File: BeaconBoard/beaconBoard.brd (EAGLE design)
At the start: 101.6 x 76.2 mm, 33 parts, among them IC1 7805TV, Q1 2N3904

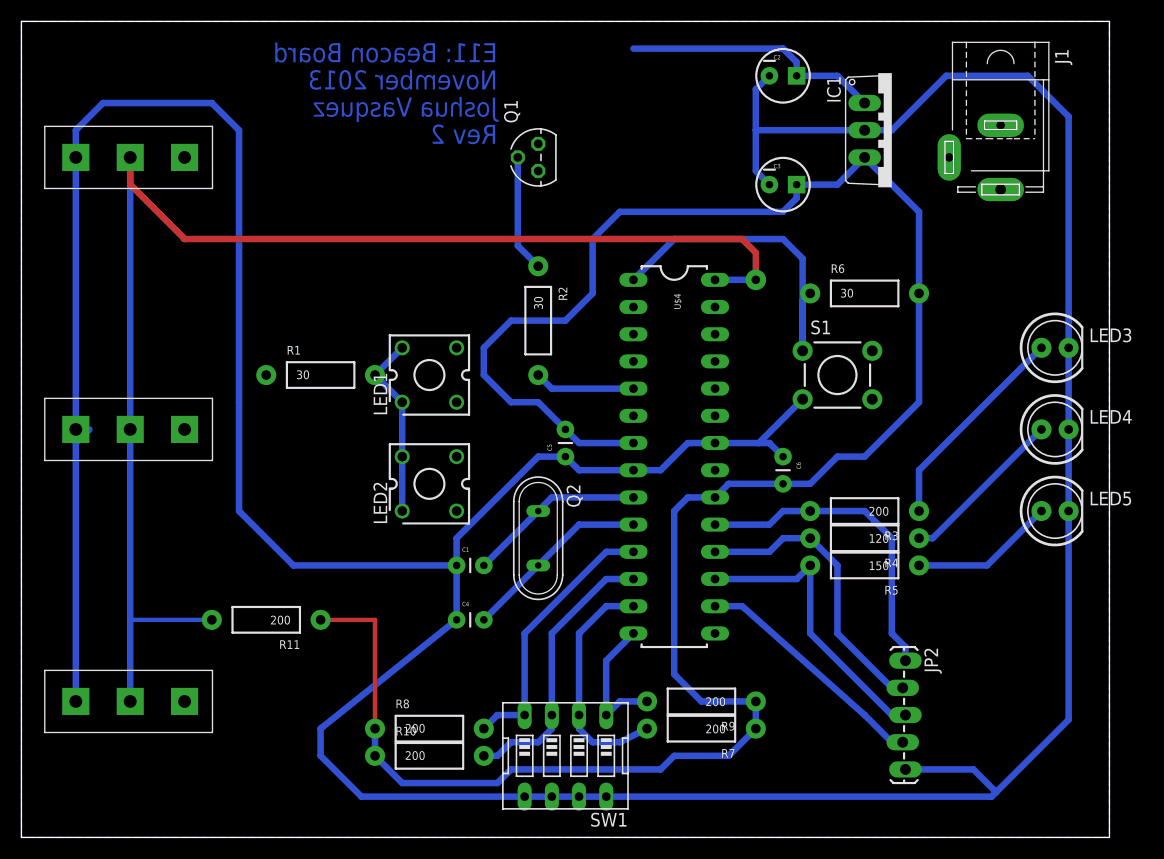
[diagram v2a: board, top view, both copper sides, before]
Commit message: Reroute for new transistor configuration
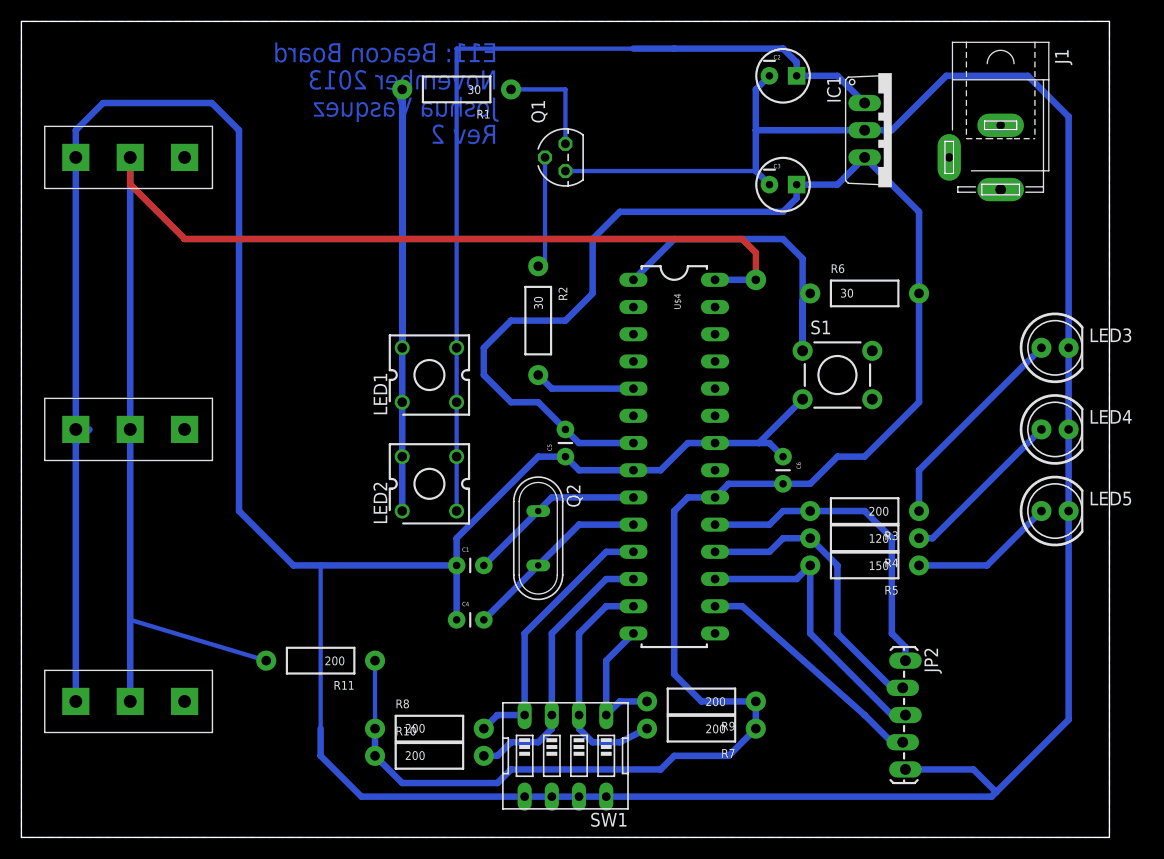
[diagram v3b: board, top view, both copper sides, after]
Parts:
- moved R1 29.5 mm to (40.6, 69.8), turned to 180 degrees
- moved R11 6.35 mm to (27.9, 16.5)
- moved Q1 2.54 mm to (50.8, 63.5)
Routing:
- net VDD: track 24.4 -> 87.9 mm
- net N$3: track 17.3 -> 63.5 mm
- net GND: track 381.3 -> 398.1 mm
- net N$1: track 0.00 -> 10.2 mm
- net VCC: track 200.8 -> 194.4 mm
- net BUMPER: track 128.4 -> 134.0 mm
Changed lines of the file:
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@@
 <element name="U$3" library="hmcfabstudio" package="D2F-L" value="DF2-L" x="5.08" y="38.1"/>
 <element name="U$4" library="hmcfabstudio" package="DIL28-3" value="ATMEGA328" x="60.96" y="35.56" rot="R270"/>
-<element name="Q1" library="transistor-small-signal" package="TO92D" value="2N3904" x="48.26" y="63.5" rot="R90"/>
+<element name="Q1" library="transistor-small-signal" package="TO92D" value="2N3904" x="50.8" y="63.5" rot="R90"/>
 <element name="J1" library="con-jack" package="SPC4078" value="" x="91.44" y="63.5" rot="R270">
 <attribute name="OC_NEWARK" value="unknown" x="91.44" y="63.5" size="1.778" layer="27" rot="R270" display="off"/>
@@
 <element name="LED1" library="led" package="CP41B" value="" x="38.1" y="43.18" rot="R90"/>
 <element name="LED2" library="led" package="CP41B" value="" x="38.1" y="33.02" rot="R90"/>
-<element name="R1" library="SparkFun-Resistors" package="AXIAL-0.4" value="30" x="27.94" y="43.18"/>
+<element name="R1" library="SparkFun-Resistors" package="AXIAL-0.4" value="30" x="40.64" y="69.85" rot="R180"/>
 <element name="R2" library="SparkFun-Resistors" package="AXIAL-0.4" value="30" x="48.26" y="48.26" rot="R270"/>
 <element name="R3" library="SparkFun-Resistors" package="AXIAL-0.4" value="200" x="78.74" y="30.48" rot="R180"/>
@@
 <element name="C6" library="SparkFun-Passives" package="CAP-PTH-SMALL" value="" x="71.12" y="35.56" rot="R270"/>
 <element name="JP2" library="SparkFun-Connectors" package="1X05_LOCK_LONGPADS" value="" x="82.55" y="16.51" rot="R270"/>
-<element name="R11" library="SparkFun-Resistors" package="AXIAL-0.4" value="200" x="22.86" y="20.32" rot="R180"/>
+<element name="R11" library="SparkFun-Resistors" package="AXIAL-0.4" value="200" x="27.94" y="16.51" rot="R180"/>
 </elements>
 <signals>
@@
 <wire x1="45.72" y1="6.35" x2="44.45" y2="5.08" width="0.6096" layer="16"/>
 <contactref element="R11" pad="P$1"/>
-<wire x1="27.94" y1="20.32" x2="33.02" y2="20.32" width="0.4064" layer="1"/>
-<wire x1="33.02" y1="20.32" x2="33.02" y2="10.16" width="0.4064" layer="1"/>
+<wire x1="33.02" y1="16.51" x2="33.02" y2="7.62" width="0.4064" layer="16"/>
 </signal>
 <signal name="GND">
@@
 <wire x1="71.12" y1="35.56" x2="69.85" y2="36.83" width="0.6096" layer="16"/>
 <wire x1="69.85" y1="36.83" x2="68.8594" y2="36.83" width="0.6096" layer="16"/>
-<wire x1="20.32" y1="40.64" x2="20.32" y2="30.48" width="0.6096" layer="16"/>
 <wire x1="20.32" y1="30.48" x2="25.4" y2="25.4" width="0.6096" layer="16"/>
-<wire x1="25.4" y1="25.4" x2="40.64" y2="25.4" width="0.6096" layer="16"/>
+<wire x1="25.4" y1="25.4" x2="27.94" y2="25.4" width="0.6096" layer="16"/>
+<wire x1="27.94" y1="25.4" x2="40.64" y2="25.4" width="0.6096" layer="16"/>
 <wire x1="40.64" y1="25.4" x2="40.64" y2="20.32" width="0.6096" layer="16"/>
-<wire x1="40.64" y1="20.32" x2="27.94" y2="10.16" width="0.6096" layer="16"/>
 <wire x1="27.94" y1="10.16" x2="27.94" y2="7.62" width="0.6096" layer="16"/>
 <wire x1="27.94" y1="7.62" x2="31.75" y2="3.81" width="0.6096" layer="16"/>
@@
 <wire x1="5.08" y1="12.7" x2="5.08" y2="36.83" width="0.6096" layer="16"/>
 <wire x1="5.08" y1="36.83" x2="6.35" y2="38.1" width="0.6096" layer="16"/>
-<wire x1="20.32" y1="40.64" x2="20.32" y2="66.04" width="0.6096" layer="16"/>
+<wire x1="20.32" y1="30.48" x2="20.32" y2="66.04" width="0.6096" layer="16"/>
 <wire x1="20.32" y1="66.04" x2="17.78" y2="68.58" width="0.6096" layer="16"/>
 <wire x1="17.78" y1="68.58" x2="7.62" y2="68.58" width="0.6096" layer="16"/>
@@
 </polygon>
 <contactref element="Q1" pad="E"/>
-<wire x1="68.58" y1="62.23" x2="48.26" y2="62.23" width="0" layer="19" extent="16-16"/>
+<wire x1="50.8" y1="62.23" x2="68.58" y2="62.23" width="0.4064" layer="16"/>
+<wire x1="27.94" y1="10.16" x2="27.94" y2="25.4" width="0.4064" layer="16"/>
 <wire x1="5.08" y1="36.83" x2="5.08" y2="38.1" width="0" layer="19" extent="16-16"/>
 </signal>
@@
 <wire x1="78.74" y1="68.58" x2="76.2" y2="71.12" width="0.6096" layer="16"/>
 <wire x1="76.2" y1="71.12" x2="72.39" y2="71.12" width="0.6096" layer="16"/>
-<wire x1="57.15" y1="73.66" x2="71.12" y2="73.66" width="0.6096" layer="16"/>
+<wire x1="57.15" y1="73.66" x2="60.96" y2="73.66" width="0.6096" layer="16"/>
+<wire x1="60.96" y1="73.66" x2="71.12" y2="73.66" width="0.6096" layer="16"/>
 <wire x1="72.39" y1="71.12" x2="72.39" y2="72.39" width="0.6096" layer="16"/>
 <wire x1="72.39" y1="72.39" x2="71.12" y2="73.66" width="0.6096" layer="16"/>
@@
 <contactref element="LED2" pad="2"/>
 <contactref element="LED2" pad="3"/>
-<wire x1="40.64" y1="45.72" x2="57.15" y2="73.66" width="0" layer="19" extent="16-16"/>
-<wire x1="40.64" y1="40.64" x2="40.64" y2="45.72" width="0" layer="19" extent="1-1"/>
+<wire x1="40.64" y1="30.48" x2="40.64" y2="45.72" width="0.4064" layer="16"/>
+<wire x1="40.64" y1="45.72" x2="40.64" y2="73.66" width="0.4064" layer="16"/>
+<wire x1="40.64" y1="73.66" x2="60.96" y2="73.66" width="0.4064" layer="16"/>
 <wire x1="40.64" y1="35.56" x2="40.64" y2="40.64" width="0" layer="19" extent="1-1"/>
-<wire x1="40.64" y1="30.48" x2="40.64" y2="35.56" width="0" layer="19" extent="1-1"/>
+<wire x1="40.64" y1="45.72" x2="40.64" y2="40.64" width="0" layer="19" extent="1-1"/>
 </signal>
 <signal name="N$3">
@@
 <contactref element="LED2" pad="1"/>
 <contactref element="R1" pad="P$2"/>
-<wire x1="33.02" y1="43.18" x2="35.56" y2="45.72" width="0.6096" layer="16"/>
-<wire x1="35.56" y1="40.64" x2="33.02" y2="43.18" width="0.6096" layer="16"/>
+<wire x1="35.56" y1="69.85" x2="35.56" y2="45.72" width="0.6096" layer="16"/>
+<wire x1="35.56" y1="40.64" x2="35.56" y2="69.85" width="0.6096" layer="16"/>
 <wire x1="35.56" y1="35.56" x2="35.56" y2="40.64" width="0.6096" layer="16"/>
 <wire x1="35.56" y1="35.56" x2="35.56" y2="30.48" width="0.6096" layer="16"/>
@@
 <contactref element="Q1" pad="B"/>
 <contactref element="R2" pad="P$1"/>
-<wire x1="48.26" y1="53.34" x2="46.355" y2="55.245" width="0.6096" layer="16"/>
-<wire x1="46.355" y1="55.245" x2="46.355" y2="63.5" width="0.6096" layer="16"/>
+<wire x1="48.26" y1="53.34" x2="48.895" y2="53.34" width="0.4064" layer="16"/>
+<wire x1="48.895" y1="53.34" x2="48.895" y2="63.5" width="0.4064" layer="16"/>
 </signal>
 <signal name="N$5">
@@
 <wire x1="10.16" y1="60.96" x2="10.16" y2="63.5" width="0.6096" layer="1"/>
 <contactref element="R11" pad="P$2"/>
-<wire x1="17.78" y1="20.32" x2="10.16" y2="20.32" width="0.4064" layer="16"/>
+<wire x1="22.86" y1="16.51" x2="10.16" y2="20.32" width="0.4064" layer="16"/>
 </signal>
 <signal name="N$1">
 <contactref element="Q1" pad="C"/>
 <contactref element="R1" pad="P$1"/>
-<wire x1="22.86" y1="43.18" x2="48.26" y2="64.77" width="0" layer="19" extent="1-1"/>
+<wire x1="45.72" y1="69.85" x2="50.8" y2="69.85" width="0.4064" layer="16"/>
+<wire x1="50.8" y1="69.85" x2="50.8" y2="64.77" width="0.4064" layer="16"/>
 </signal>
 </signals>
